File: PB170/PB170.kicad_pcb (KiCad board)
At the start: 2 copper layers, 30 parts, among them J1 USB_C_Receptacle_USB2.0-Conne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, J2 USB_B_Micro, Q1 P-MOSFET-MLP_HS, Q2 BC817, SW1 SW_MEC_5E, SW2 SW_MEC_5E, U1 74HC00

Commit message: Added PCB.
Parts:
- added H1: MountingHole_Pad, Mounting_Holes:MountingHole_3.2mm_M3_Pad, F.Cu at (45.7, 30.5)
- added H2: MountingHole_Pad, Mounting_Holes:MountingHole_3.2mm_M3_Pad, F.Cu at (45.7, 91.4)
- added H3: MountingHole_Pad, Mounting_Holes:MountingHole_3.2mm_M3_Pad, F.Cu at (132.1, 30.5)
- added H4: MountingHole_Pad, Mounting_Holes:MountingHole_3.2mm_M3_Pad, F.Cu at (132.1, 91.4)
- J1, J2: moved to B.Cu
- moved D5 88.3 mm to (120.7, 92.7)
- moved D4 84.4 mm to (102.1, 92.7)
- moved D6 83.8 mm to (111.3, 92.7)
- moved D2 83.5 mm to (131.3, 83.8)
- moved R7 78.5 mm to (119.4, 88.9)
- moved R2 77.4 mm to (127.0, 83.8), turned to 180 degrees
- moved Q2 76.0 mm to (111.8, 74.9), turned to 90 degrees
- moved R3 73.8 mm to (126.5, 77.5)
- moved R12 73.8 mm to (108.0, 76.2), turned to 180 degrees
- moved D3 73.5 mm to (122.4, 77.5), turned to 180 degrees
- moved R8 73.1 mm to (111.0, 88.9)
- moved R6 72.8 mm to (102.3, 88.9)
- moved C3 70.7 mm to (53.3, 77.5), turned to 90 degrees
- moved R4 70.0 mm to (48.3, 77.5), turned to 90 degrees
- moved C4 63.8 mm to (53.3, 64.8), turned to 90 degrees
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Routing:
- net GND: track 0.00 -> 32.0 mm, vias 0 -> 4
- net Net-(U1-Pad3): track 0.00 -> 8.96 mm, vias 0 -> 2
- net Net-(U1-Pad12): track 0.00 -> 6.71 mm
- net +5V: track 0.00 -> 4.68 mm
- net Net-(J2-Pad3): track 0.00 -> 3.47 mm, vias 0 -> 1
- net Net-(R12-Pad2): track 0.00 -> 3.16 mm
- net Net-(J2-Pad2): track 0.00 -> 3.11 mm, vias 0 -> 1
- net Net-(Q2-Pad1): track 0.00 -> 2.22 mm
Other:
- board outline added: 96.5 x 71.1 mm
- copper layers 2 -> 4
- rule via_min_drill: 0.3 -> 0.2
- rule via_min_size: 0.4 -> 0.45

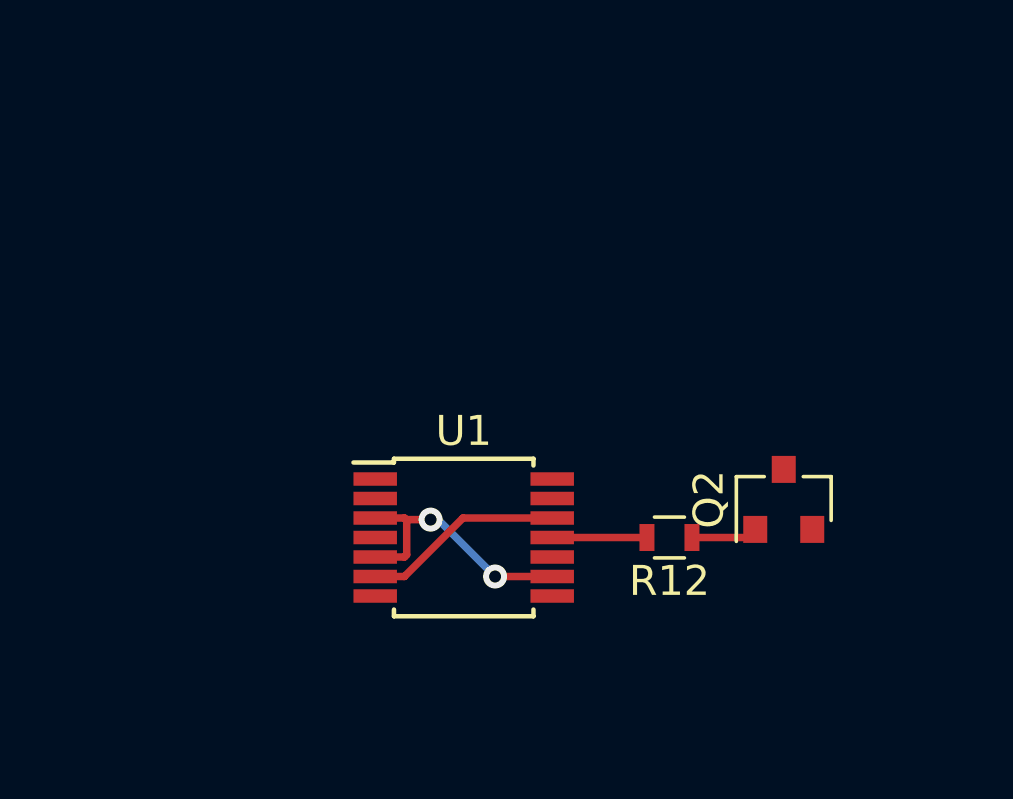
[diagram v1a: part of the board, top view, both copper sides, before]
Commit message: Added hierarchical sheet example.
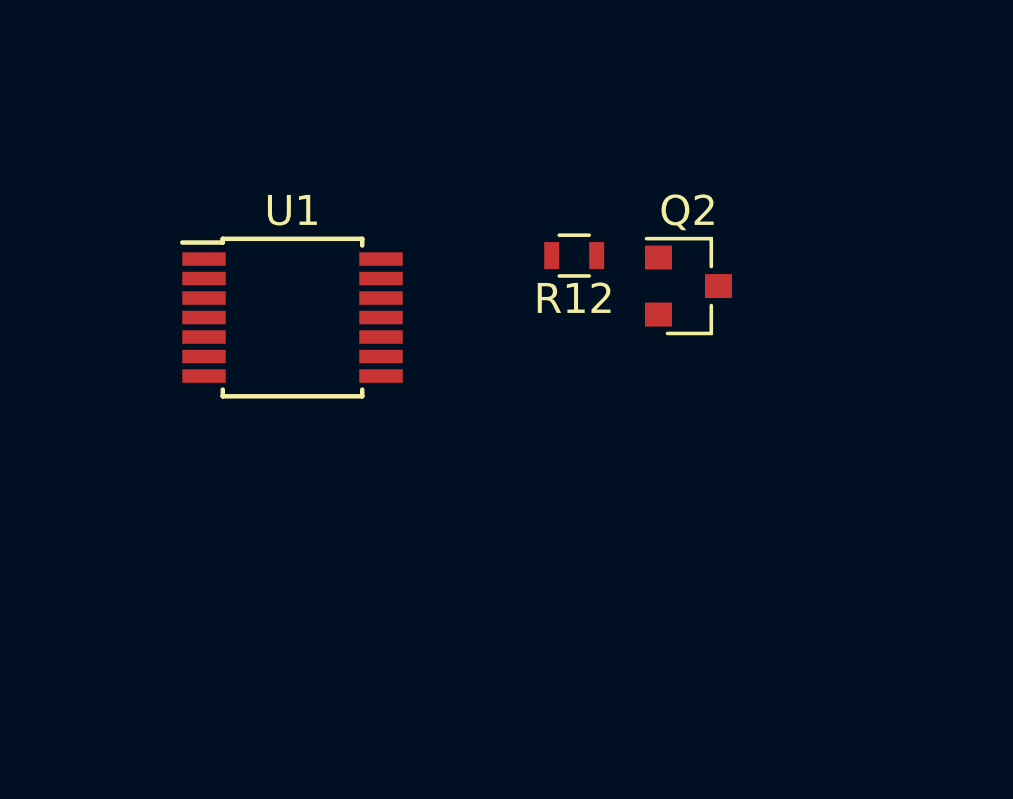
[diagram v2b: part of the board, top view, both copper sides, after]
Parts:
- moved R12 9.92 mm to (104.8, 66.8)
- moved U1 9.29 mm to (95.4, 68.9)
- moved Q2 7.79 mm to (108.6, 67.8), turned to 0 degrees
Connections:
- net Net-(C3-Pad1) renamed /SheetXOR/IN_A
- net Net-(C4-Pad1) renamed /SheetXOR/IN_B
- net Net-(R12-Pad2) renamed OUTPUT
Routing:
- net Net-(U1-Pad3): track 8.96 -> 0.00 mm, vias 2 -> 0
- net Net-(U1-Pad12): track 6.71 -> 0.00 mm
- net OUTPUT: track 3.16 -> 0.00 mm
- net Net-(Q2-Pad1): track 2.22 -> 0.00 mm
